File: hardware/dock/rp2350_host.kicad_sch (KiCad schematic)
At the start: 0 parts

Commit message: Dock schematic: review fixes, Pico 2/XIAO socket+pogo mounting
- Cross HID UART TX/RX; split ROLE_STRAP per endpoint
- VBUS sense (GP4) and USB-C CC current sensing (GP26/27) on HID endpoints
- Pogo +5V via TPS2552 enabled by DET, TPD4E1U06 ESD + 1k on pogo lines
- 2x100uF bulk on SYS_5V and keyboard VBUS; 100k EN pull-down
- Remove TPS62162 rail: XIAO from 5V, pull-ups on module 3V3 rails
- Socketed Pico 2 / XIAO footprints with P50-B1 probe holes for USB+SWD
- XIAO SWD header J8; RP2350 reset control of HID/BLE endpoints
- DESIGN.md: UART allocation, power budget, mounting, reset control
- Add .gitignore, custom libraries and datasheets

Co-Authored-By: Claude Opus 5.5 <noreply@anthropic.com>
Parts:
- added A1: RaspberryPi_Pico, dock:RaspberryPi_Pico2_Socket_Pogo, symbol MCU_Module:RaspberryPi_Pico_Extensive
- added J2: Conn_01x05_Pin, Connector_PinHeader_2.54mm:PinHeader_1x05_P2.54mm_Vertical, symbol Connector:Conn_01x05_Pin
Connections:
- new net: A1.30 (RUN), J2.4 (Pin_4)
- new net: A1.D1 (SWCLK), J2.1 (Pin_1)
- new net: A1.D3 (SWDIO), J2.2 (Pin_2)
- new net BLE_RST_CTRL: A1.29 (GPIO22)
- new net BLE_UART_RX: A1.12 (GPIO9)
- new net BLE_UART_TX: A1.11 (GPIO8)
- new net GND: A1.13 (GND), A1.18 (GND), A1.23 (GND), A1.28 (GND), A1.3 (GND), A1.33 (AGND), A1.38 (GND), A1.8 (GND), A1.D2 (GND), A1.TP1 (USB_GND), J2.3 (Pin_3)
- new net HID_PERSONAL_RUN_CTRL: A1.25 (GPIO19)
- new net HID_PERSONAL_RX: A1.2 (GPIO1)
- new net HID_PERSONAL_TX: A1.1 (GPIO0)
- new net HID_WORK_RUN_CTRL: A1.27 (GPIO21)
- new net HID_WORK_RX: A1.7 (GPIO5)
- new net HID_WORK_TX: A1.6 (GPIO4)
- new net HOST_3V3: A1.36 (3V3), J2.5 (Pin_5)
- new net KEYBOARD_VBUS_EN: A1.21 (GPIO16)
- new net KEYBOARD_VBUS_FAULT: A1.22 (GPIO17)
- new net MUX_STATUS: A1.24 (GPIO18)
- new net POGO_5V_FAULT: A1.26 (GPIO20)
- new net SYS_5V: A1.39 (VSYS)
- new net USB_HOST_DM: A1.TP2 (USB_DM)
- new net USB_HOST_DP: A1.TP3 (USB_DP)
- no-connect marks 0 -> 19

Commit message: Net classes, project lib tables, docs and datasheets; PCB synced
- Rename USB pairs to *_D_P/*_D_N; add Power and USB net classes
- Project-relative fp-lib-table and new sym-lib-table
- Pico values set to "Raspberry Pi Pico 2"; J1 symbol synced with library
- DESIGN.md/README: Pico 2 x3 + XIAO modules, TPS2116, pogo switch/ESD,
  VBUS/CC sensing, SWD pinout, resolved and open items
- Add TPS2552/2553, TPD2EUSB30 and P50 probe datasheets
- PCB updated from schematic (F8)

Co-Authored-By: Claude Opus 5.5 <noreply@anthropic.com>
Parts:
- A1: value RaspberryPi_Pico -> Raspberry Pi Pico 2
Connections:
- net USB_HOST_DM renamed USB_HOST_D_N
- net USB_HOST_DP renamed USB_HOST_D_P

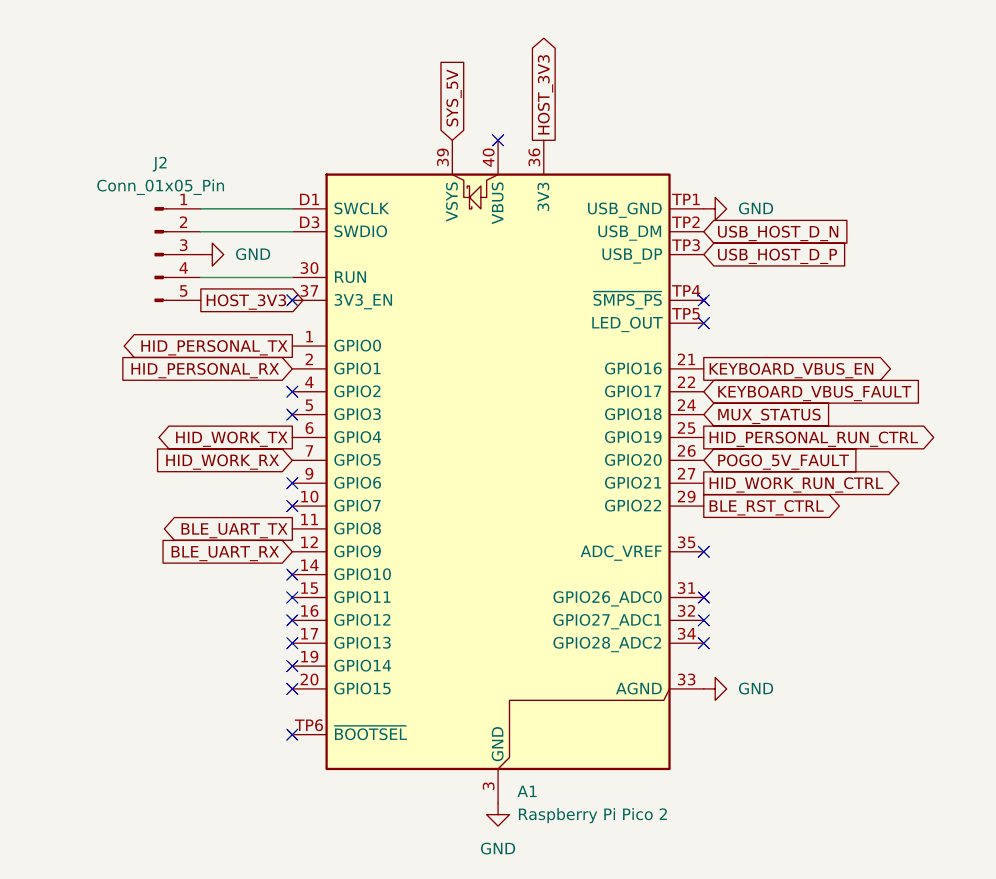
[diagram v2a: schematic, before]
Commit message: Re-pin host/endpoint GPIOs by PCB position; update placement guide
- Host A1: HID-A UART0 -> GP12/13, HID-B UART1 -> GP20/21, BLE PIO ->
  GP16/17, KEYBOARD_VBUS_EN/FAULT -> GP26/27, MUX_STATUS -> GP28,
  POGO_5V_FAULT -> GP18, HID_PERSONAL_RUN_CTRL -> GP2,
  HID_WORK_RUN_CTRL -> GP19 (BLE_RST_CTRL stays GP22)
- HID-A UART0 -> GP16/17, HID-B UART0 -> GP12/13 (pins facing the host)
- Ratsnest crossings on current placement 132 -> 95
- DESIGN.md pin tables updated; PCB_PLACEMENT.md: pull-up/pull-down
  placement, Pico GPIO map, 100x100 outline, routing techniques
- Stop tracking KiCad _restore_backup_* folders (kept on disk, ignored)

Co-Authored-By: Claude Opus 5.5 <noreply@anthropic.com>
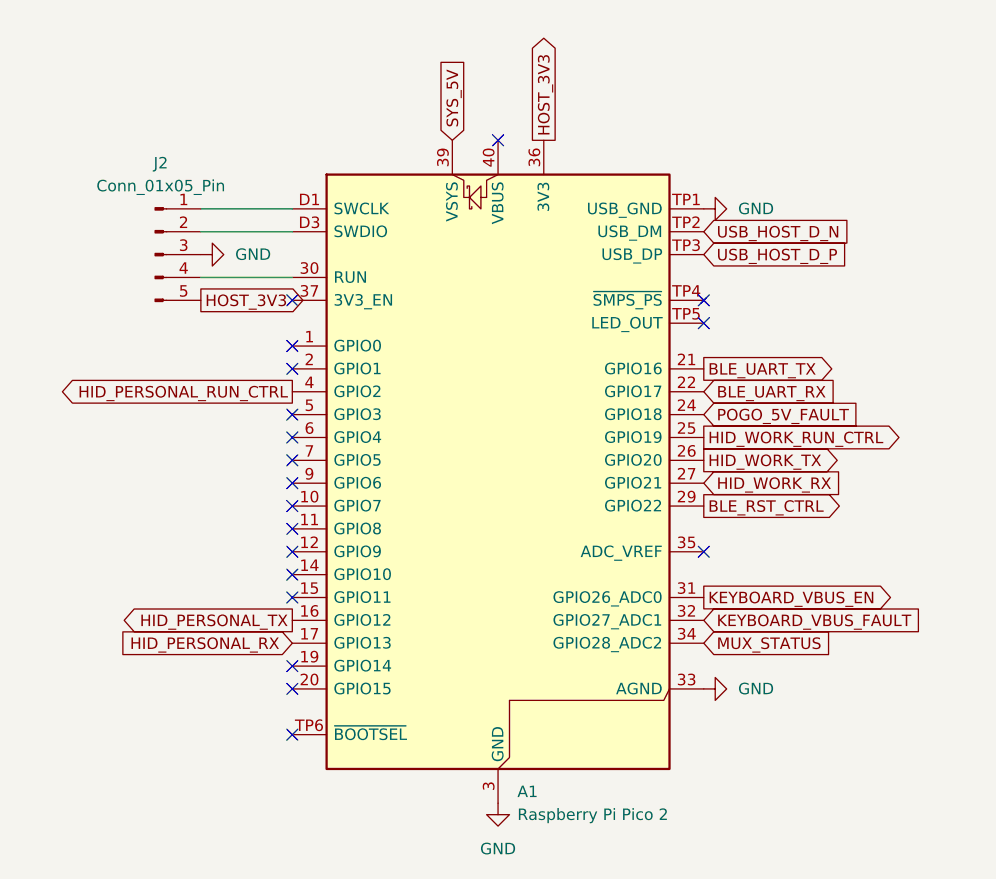
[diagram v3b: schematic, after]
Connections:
- net BLE_UART_RX: now also A1.22 (GPIO17); no longer A1.12 (GPIO9)
- net BLE_UART_TX: now also A1.21 (GPIO16); no longer A1.11 (GPIO8)
- net HID_PERSONAL_RUN_CTRL: now also A1.4 (GPIO2); no longer A1.25 (GPIO19)
- net HID_PERSONAL_RX: now also A1.17 (GPIO13); no longer A1.2 (GPIO1)
- net HID_PERSONAL_TX: now also A1.16 (GPIO12); no longer A1.1 (GPIO0)
- net HID_WORK_RUN_CTRL: now also A1.25 (GPIO19); no longer A1.27 (GPIO21)
- net HID_WORK_RX: now also A1.27 (GPIO21); no longer A1.7 (GPIO5)
- net HID_WORK_TX: now also A1.26 (GPIO20); no longer A1.6 (GPIO4)
- net KEYBOARD_VBUS_EN: now also A1.31 (GPIO26_ADC0); no longer A1.21 (GPIO16)
- net KEYBOARD_VBUS_FAULT: now also A1.32 (GPIO27_ADC1); no longer A1.22 (GPIO17)
- net MUX_STATUS: now also A1.34 (GPIO28_ADC2); no longer A1.24 (GPIO18)
- net POGO_5V_FAULT: now also A1.24 (GPIO18); no longer A1.26 (GPIO20)

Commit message: Host becomes Pico 2 W (on-board BLE); remove XIAO nRF52840
- A1 -> Raspberry Pi Pico 2 W, new footprint RaspberryPi_Pico2W_Socket_Pogo
  (TP1-3 probes unchanged, SWD via 1x3 socket under the debug holes,
  TP4-6 at Pico 2 W positions, 14x9 mm antenna keep-out)
- Remove U7 (XIAO), J8 and R35; BLE UART and BLE_RST_CTRL gone
- Pogo TX/RX/DET now go to the host: GP16 (PIO TX), GP17 (PIO RX),
  GP22 (DET); R18 pulls DET up to HOST_3V3
- HID-A: CC1/CC2 on U5 and R29/R30 swapped for routing (user change)
- DESIGN.md/README/PCB_PLACEMENT.md updated; board includes in-progress
  routing and B.Cu GND zone (not yet updated from schematic)

Co-Authored-By: Claude Opus 5.5 <noreply@anthropic.com>
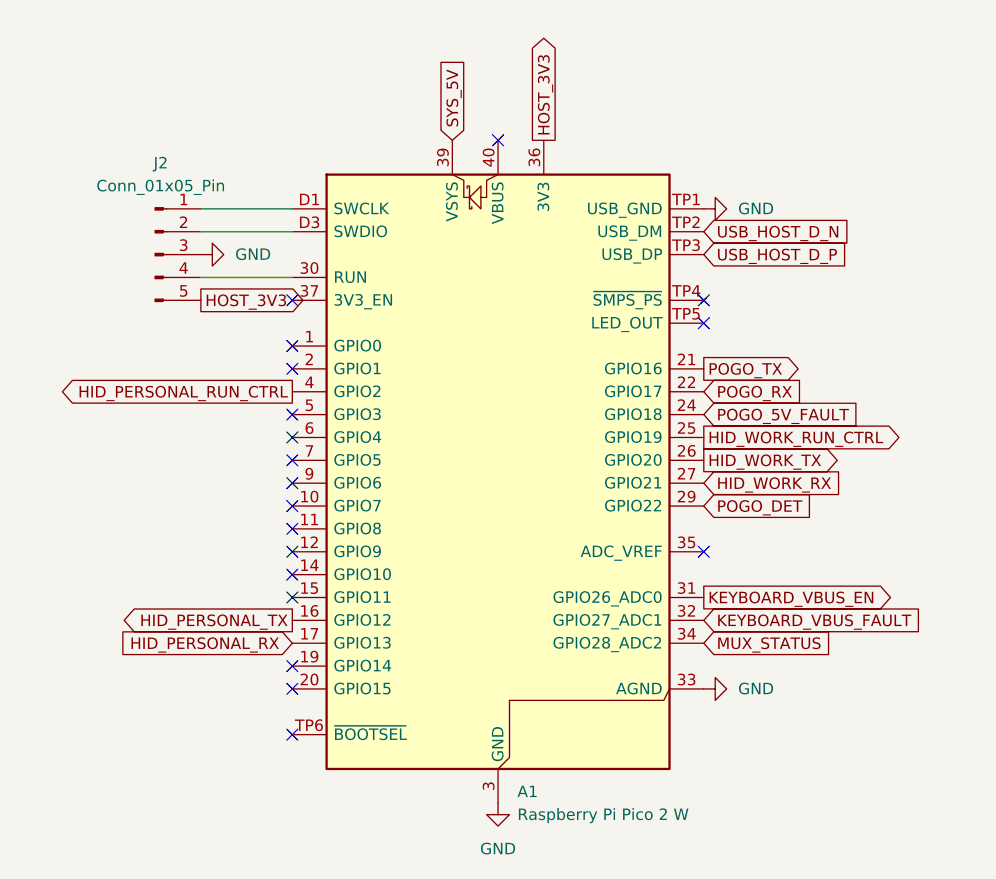
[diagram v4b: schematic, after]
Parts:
- A1: value Raspberry Pi Pico 2 -> Raspberry Pi Pico 2 W; footprint dock:RaspberryPi_Pico2_Socket_Pogo -> dock:RaspberryPi_Pico2W_Socket_Pogo
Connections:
- net BLE_RST_CTRL renamed POGO_DET
- net BLE_UART_RX renamed POGO_RX
- net BLE_UART_TX renamed POGO_TX
